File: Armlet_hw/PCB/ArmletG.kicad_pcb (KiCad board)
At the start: 2 copper layers, 93 x 35 mm, 86 parts, among them M1 MOTOR_NO_CONTACTS, Q1 LED_RGB 5050, Q2 BC848, Q3 MMBT2222, Q5 MMBT2222, SW1 DIPx6, SW2 BUTTON, SW4 SWITCH

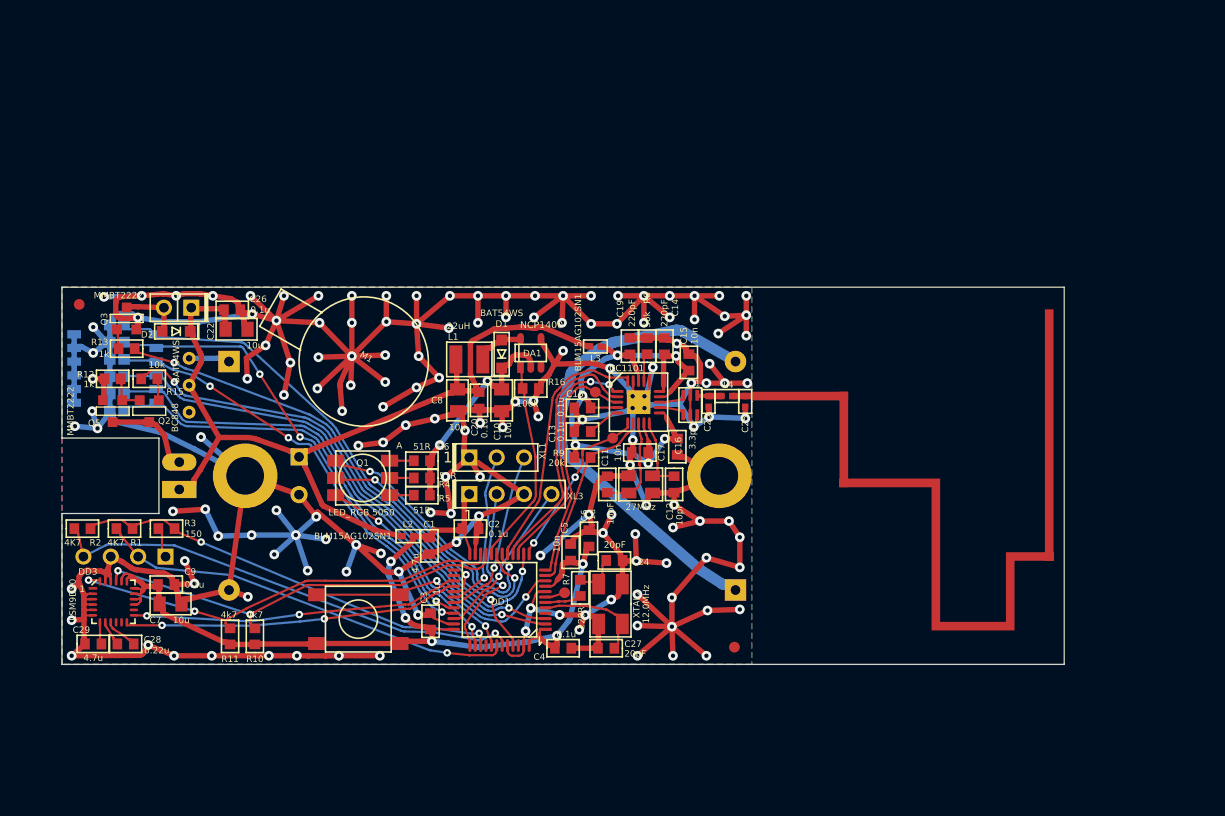
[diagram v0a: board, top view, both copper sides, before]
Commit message: 3 parts of armlet case
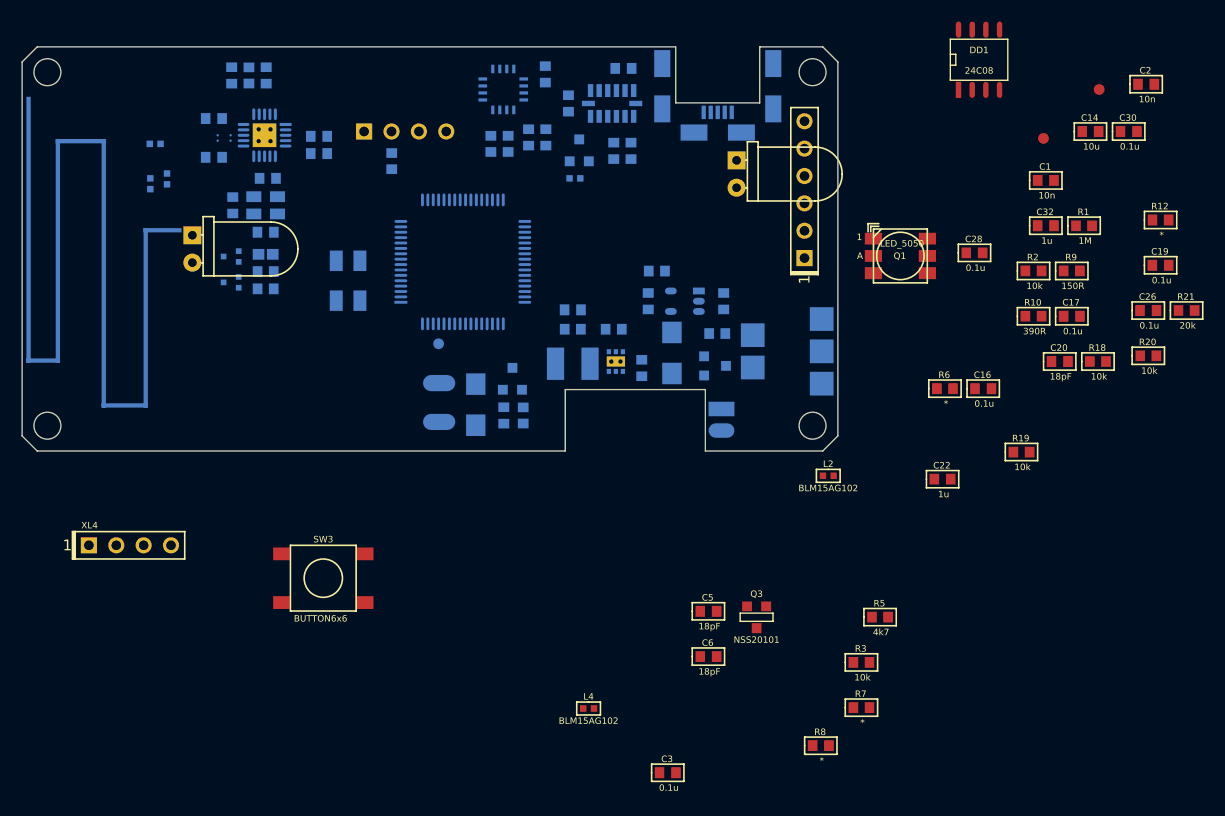
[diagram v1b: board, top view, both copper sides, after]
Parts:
- removed B1, B2: BAT, Installations:BATTERY_AAA_X1
- removed C23: 1.5pF, Capacitors:CAP_0402
- removed F2, F3, F4, F5, F6: Fuse0R, Resistors:RES_0603_FUSE
- removed HOLE1, HOLE2: HOLE_METALLED, PCB:Hole3_5_out6mm
- removed R15: 10k, Resistors:RES_0603
- removed RP1, RP2: REFPOINT, PCB:REF_POINT_1MM
- removed SW1: DIPx6, Switches:DIP_SMD_1D27X6
- removed SW2: BUTTON, Switches:BTN_6x6
- removed SW4: SWITCH, Switches:SW_SS-1P2T
- added C30: 0.1u, Capacitors:CAP_0603, F.Cu at (190.0, 76.1)
- added C31: 0.1u, Capacitors:CAP_0603, B.Cu at (143.8, 77.8)
- added C32: 1u, Capacitors:CAP_0603, F.Cu at (182.3, 84.8)
- added C33: 220pF, Capacitors:CAP_0603, B.Cu at (106.8, 70.8)
- added C34: *, Capacitors:CAP_0402, B.Cu at (99.7, 77.2)
- added C35: 10n, Capacitors:CAP_0603, B.Cu at (105.1, 74.8)
- added C36: 3.3pF, Capacitors:CAP_0603, B.Cu at (105.1, 78.5)
- added C37: *, Capacitors:CAP_0402, B.Cu at (100.8, 80.5)
- added C38: 10n, Capacitors:CAP_0603, B.Cu at (110.1, 80.4)
- added C39: 0.1u, Capacitors:CAP_0603, B.Cu at (114.8, 76.5)
- added C40: 220pF, Capacitors:CAP_0603, B.Cu at (110.0, 70.8)
- added D4: LED, LEDs:LED_Through-Hole-5mm-HOR, F.Cu at (103.1, 87.0)
- added DA2: NCP1529DFN, QFN_DFN:DFN6, B.Cu at (142.4, 97.4)
- added DD4: LSM303DLHC, LGA:14_5X3_P08, B.Cu at (142.1, 73.5)
- added DD5: CC1101, QFN_DFN:QFN20, B.Cu at (109.8, 76.4)
- added L5: *, Inductors:IND_0402, B.Cu at (99.2, 80.9)
- added Q4: IRLML9303, SOT:SOT23-3, B.Cu at (151.6, 97.8)
- added Q7: NSS20101, SOT:SC89-3, B.Cu at (106.7, 90.1)
- added Q8: NSS20101, SOT:SC89-3, B.Cu at (106.7, 87.7)
- added R14: 4k7, Resistors:RES_0603, B.Cu at (130.8, 77.2)
- added R17: 10k, Resistors:RES_0603, B.Cu at (151.8, 94.8)
- added R18: 10k, Resistors:RES_0603, F.Cu at (187.1, 97.4)
- added R19: 10k, Resistors:RES_0603, F.Cu at (180.0, 105.8)
- added R20: 10k, Resistors:RES_0603, F.Cu at (191.8, 96.9)
- added R21: 20k, Resistors:RES_0603, F.Cu at (195.4, 92.7)
- added R22: 390k, Resistors:RES_0603, B.Cu at (138.4, 94.4)
- added R23: 100k, Resistors:RES_0603, B.Cu at (142.2, 94.4)
- added R25: 56k, Resistors:RES_0603, B.Cu at (108.3, 70.8)
- added R26: 10k, Resistors:RES_0603, B.Cu at (109.9, 89.1)
- added R27: 1k, Resistors:RES_0603, B.Cu at (109.9, 90.7)
- added SW3: BUTTON6x6, BtnsSwitches:BTN_6x6, F.Cu at (115.2, 117.5)
- added XL2: CONN_4, Connectors:PBS-4R, B.Cu at (122.8, 76.1)
- added XL5: NOKIA_BAT, Connectors:CONN_NOKIA_ACC, B.Cu at (156.3, 96.5)
- added XL7: CONN_1, PCB:Oval3x1.5, B.Cu at (126.0, 99.4)
- ANT1: footprint Radio:ANT_868_MEANDER_4HOR_35mm -> Radio:ANT_868_ARMLETG; moved to B.Cu
- BLN1: value 0896BM15A0001 -> BALUN868ST; footprint Radio:BALUN_JOHANSON868 -> Radio:BALUN868_ST; moved to B.Cu
- C1: value 4.7u -> 10n
- C10: value 10u -> 10n; footprint Capacitors:CAP_0805 -> Capacitors:CAP_0603; moved to B.Cu
- C11: value 10pF -> 4.7u; moved to B.Cu
- C12: value 10pF -> 10u; moved to B.Cu
- C13, TP1: moved to B.Cu
- C14: value 220pF -> 10u
- C15: value 10n -> 18pF; moved to B.Cu
- C16: value 3.3pF -> 0.1u
- C17: value 10n -> 0.1u
- C18: value 0.1u -> 18pF; moved to B.Cu
- C19: value 220pF -> 0.1u
- C2: value 0.1u -> 10n
- C20: value 0.1u -> 18pF
- C21: value 1000u 6v3 -> 0.1u; footprint Capacitors:CAP_08xxR_HOR -> Capacitors:CAP_0603
- C22: value 10u -> 1u; footprint Capacitors:CAP_0805 -> Capacitors:CAP_0603
- C24: value 20pF -> 10u; moved to B.Cu
- C25: value DoNotMount -> 0.22u; footprint Capacitors:CAP_0402 -> Capacitors:CAP_0603; moved to B.Cu
- C27: value 20pF -> 4.7u; moved to B.Cu
- C28: value 0.22u -> 0.1u
- C29: value 4.7u -> 10u; moved to B.Cu
- C4: value 0.1u -> 4.7u; moved to B.Cu
- C5: value 10n -> 18pF
- C6: value 1u -> 18pF
- C7: value 10u -> 4.7u; footprint Capacitors:CAP_0805 -> Capacitors:CAP_0603; moved to B.Cu
- C8: value 10u -> 220u16V; footprint Capacitors:CAP_0805 -> Capacitors:CAP_05xxR_horiz_HOLE; moved to B.Cu
- C9: value 0.1u -> 10u; moved to B.Cu
- D1: value BAT54WS -> WhiteLED; footprint Diodes:SOD323 -> LEDs:LED_Through-Hole-5mm-HOR
- D2: value BAT54WS -> SS14; footprint Diodes:SOD323 -> Diodes:SMA_DO214AC; moved to B.Cu
- D3: value LED -> SS14; footprint LEDs:LED_SMD-5mm-HOR_mirr -> Diodes:SMA_DO214AC
- DA1: value NCP1400 -> MCP73832; moved to B.Cu
- DD1: value STM32L151CxTx -> 24C08; footprint LQFP:LQFP48 -> SO_DIL_TSSOP:SO8_150MIL
- DD2: value CC1101 -> STM32L476Rx; footprint QFN:QFN20 -> LQFP_TQFP:LQFP64; moved to B.Cu
- DD3: value LSM9DS0 -> L3GD20; footprint LGA:24_4X4_P05 -> LGA:16_4X4_P065; moved to B.Cu
- L1: value 22uH -> BLM15AG102; footprint Inductors:IND_1210_LQH32C -> Inductors:IND_0402; moved to B.Cu
- L2: value BLM15AG102SN1 -> BLM15AG102
- L3: value BLM15AG102SN1 -> 2.2uH; footprint Inductors:IND_0402 -> Inductors:IND_1515; moved to B.Cu
- L4: value 5.6nH -> BLM15AG102
- M1: footprint PCB:Motor_no_Contacts -> Installation:Motor_no_Contacts; moved to B.Cu
- Q1: value LED_RGB 5050 -> LED_5050; footprint LEDs:5050 -> LEDs:LED_5050
- Q2: value BC848 -> IRLML9303; moved to B.Cu
- Q3: value MMBT2222 -> NSS20101
- Q5: value MMBT2222 -> NSS20101; moved to B.Cu
- R1: value 4K7 -> 1M
- R10: value 4k7 -> 390R
- R11: value 4k7 -> 2k; moved to B.Cu
- R12: value 1k -> *
- R13: value 1k -> 4k7; moved to B.Cu
- R16: value 100k -> 1k; moved to B.Cu
- R2: value 4K7 -> 10k
- R3: value 150 -> 10k
- R4: value 51R -> 4k7; moved to B.Cu
- R5: value 51R -> 4k7
- R6: value 51R -> *
- R7: value 220R -> *
- R8: value 56k -> *
- R9: value 20k -> 150R
- XL1: value CONN_3 -> CONN_6; footprint Connectors:PLS-3 -> Connectors:PLS-6; moved to B.Cu
- XL3: value ST_SWD -> USB_Micro_B; footprint Connectors:PLS-4 -> Connectors:USBmicro_MOLEX_WM17142; moved to B.Cu
- XL4: footprint Connectors:PBS-4R -> Connectors:PLS-4; moved to F.Cu
- XL6: value CONN_2 -> CONN_1; footprint Connectors:PLS-2 -> PCB:Oval3x1.5; moved to B.Cu
- XTAL1: value 27MHz -> 12MHz; footprint Quartz:03225C4 -> Quartz:0503x4-4; moved to B.Cu
- XTAL2: value 12.0MHz -> 27MHz; footprint Quartz:0503x4-4 -> Quartz:03225C4; moved to B.Cu
- moved R12 98.4 mm to (192.9, 84.3)
- moved R1 93.4 mm to (185.8, 84.8)
- moved R2 91.4 mm to (181.2, 89.0)
- moved C28 86.7 mm to (175.7, 87.3), turned to 0 degrees
- moved C26 85.0 mm to (191.8, 92.7)
- moved R10 78.1 mm to (181.2, 93.2), turned to 0 degrees
- moved C2 75.0 mm to (191.6, 71.7)
- moved DD1 67.0 mm to (176.1, 69.4), turned to 0 degrees
- moved C22 67.0 mm to (172.7, 108.3)
- moved C29 66.5 mm to (142.2, 77.8), turned to 90 degrees
- moved C1 66.5 mm to (182.3, 80.6), turned to 0 degrees
- moved R3 65.7 mm to (165.2, 125.3)
- moved Q3 64.7 mm to (155.5, 121.1), turned to 0 degrees
- moved DD3 59.7 mm to (131.9, 72.2), turned to 90 degrees
- moved C7 58.5 mm to (152.4, 91.8), turned to 270 degrees
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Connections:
- C1 pad 1: PwrMCU -> GND
- C1 pad 2: GND -> /SHLD
- C10 pad 1: +3.3V -> GND
- C10 pad 2: GND -> Net-(C10-Pad2)
- C11 pad 1: Net-(C11-Pad1) -> GND
- C11 pad 2: GND -> PwrUnst
- C12 pad 1: Net-(C12-Pad1) -> GND
- C12 pad 2: GND -> /PWR_ACC
- C13 pad 1: Net-(C13-Pad1) -> GND
- C13 pad 2: GND -> /PWR_ACC
- C14 pad 1: VCC -> GND
- C14 pad 2: GND -> PwrMCU
- C15 pad 1: VCC -> Net-(C15-Pad1)
- C16 pad 1: VCC -> GND
- C16 pad 2: GND -> PwrMCU
- C17 pad 1: VCC -> GND
- C17 pad 2: GND -> PwrMCU
- C18 pad 1: VCC -> Net-(C18-Pad1)
- C19 pad 1: VCC -> GND
- C19 pad 2: GND -> PwrMCU
- C2 pad 1: PwrMCU -> GND
- C2 pad 2: GND -> +5V
- C20 pad 1: +BATT -> Net-(C20-Pad1)
- C20 pad 2: GND -> +3.3V
- C21 pad 1: +BATT -> GND
- C21 pad 2: GND -> Net-(C21-Pad2)
- C22 pad 1: +BATT -> GND
- C22 pad 2: GND -> PwrMCU
- C24 pad 1: Net-(C24-Pad1) -> GND
- C24 pad 2: GND -> +3.3V
- C25 pad 1: /ANT2 -> Net-(C25-Pad1)
- C25 pad 2: GND -> Net-(C25-Pad2)
- C26 pad 1: +BATT -> GND
- C26 pad 2: GND -> PwrMCU
- C27 pad 1: Net-(C27-Pad1) -> GND
- C27 pad 2: GND -> Net-(C27-Pad2)
- C28 pad 1: Net-(C28-Pad1) -> GND
- C28 pad 2: Net-(C28-Pad2) -> PwrMCU
- C29 pad 2: Net-(C29-Pad2) -> /PWR_ACC
- C3 pad 1: PwrMCU -> GND
- C3 pad 2: GND -> /PWR_EE
- C4 pad 1: PwrMCU -> GND
- C4 pad 2: GND -> +5V
- C5 pad 1: PwrMCU -> Net-(C5-Pad1)
- C6 pad 1: PwrMCU -> Net-(C6-Pad1)
- C7 pad 1: PwrMCU -> GND
- C7 pad 2: GND -> +BATT
- C9 pad 1: PwrMCU -> GND
- C9 pad 2: GND -> +3.3V
- D1 pad A: /Lout -> PwrUnst
- D1 pad C: +3.3V -> Net-(D1-PadC)
- D2 pad A: /VibroOut -> +5V
- D2 pad C: +BATT -> PwrUnst
- D3 pad A: +BATT -> /VIBRO_OUT
- D3 pad C: /IR_LED_OUT -> +3.3V
- DA1 pad 1: /LED_EN -> /Charge
- DA1 pad 2: +3.3V -> GND
- DA1 pad 3: (no net) -> +BATT
- DA1 pad 4: GND -> +5V
- DA1 pad 5: /Lout -> Net-(DA1-Pad5)
- DD1 pad 1: PwrMCU -> GND
- DD1 pad 2: /DS2 -> GND
- DD1 pad 3: /DS3 -> GND
- DD1 pad 4: (no net) -> GND
- DD1 pad 5: Net-(C27-Pad1) -> /SDA_EE
- DD1 pad 6: Net-(DD1-Pad6) -> /SCL_EE
- DD1 pad 7: Net-(DD1-Pad7) -> GND
- DD1 pad 8: GND -> /PWR_EE
- DD2 pad 1: /CC_SCK -> PwrMCU
- DD2 pad 10: Net-(C12-Pad1) -> /PWR_EE
- DD2 pad 11: VCC -> (no net)
- DD2 pad 12: /RF1 -> GND
- DD2 pad 13: /RF2 -> PwrMCU
- DD2 pad 14: VCC -> /CC_GDO0
- DD2 pad 15: VCC -> /CC_CS
- DD2 pad 16: GND -> /UART_TX
- DD2 pad 17: Net-(DD2-Pad17) -> /UART_RX
- DD2 pad 18: VCC -> GND
- DD2 pad 19: GND -> PwrMCU
- DD2 pad 2: /CC_MISO -> Net-(DD2-Pad2)
- DD2 pad 20: /CC_MOSI -> /IR_OUT_DAC
- DD2 pad 3: /CC_GDO2 -> (no net)
- DD2 pad 4: VCC -> (no net)
- DD2 pad 5: Net-(C13-Pad1) -> Net-(C5-Pad1)
- DD2 pad 6: /CC_GDO0 -> Net-(DD2-Pad6)
- DD2 pad 7: /CC_CS -> Net-(DD2-Pad7)
- DD2 pad 8: Net-(C11-Pad1) -> /SCL_EE
- DD2 pad 9: VCC -> /SDA_EE
- DD3 pad 1: (no net) -> /PWR_ACC
- DD3 pad 10: (no net) -> GND
- DD3 pad 11: (no net) -> GND
- DD3 pad 12: /GYRO_DRDY -> GND
- DD3 pad 13: /ACC_INT1 -> GND
- DD3 pad 14: (no net) -> Net-(C10-Pad2)
- DD3 pad 15: PwrMCU -> /PWR_ACC
- DD3 pad 16: PwrMCU -> /PWR_ACC
- DD3 pad 2: GND -> /SCL_ACC
- DD3 pad 3: GND -> /SDA_ACC
- DD3 pad 4: GND -> /PWR_ACC
- DD3 pad 5: GND -> /PWR_ACC
- DD3 pad 6: GND -> /GYRO_DRDY
- DD3 pad 7: Net-(C29-Pad2) -> (no net)
- DD3 pad 8: Net-(C28-Pad2) -> GND
- DD3 pad 9: Net-(C28-Pad1) -> GND
- F1 pad 1: /DS1 -> Net-(F1-Pad1)
- F1 pad 2: GND -> /IR_OUT_TIM
- L1 pad 1: /Lout -> Net-(L1-Pad1)
- L1 pad 2: +BATT -> +3.3V
- L2 pad 2: +BATT -> +3.3V
- L3 pad 1: VCC -> +3.3V
- L3 pad 2: +BATT -> /Lout3V3
- L4 pad 1: /ANT2 -> VCC
- L4 pad 2: /ANT1 -> +3.3V
- Q2 pad 1: Net-(Q2-Pad1) -> /PWR_ACC_CTRL
- Q2 pad 2: Net-(Q2-Pad2) -> Net-(L1-Pad1)
- Q2 pad 3: /IR_LED_OUT -> /PWR_ACC
- Q3 pad 3: /VibroOut -> Net-(D1-PadC)
- Q5 pad 1: Net-(Q2-Pad2) -> Net-(Q5-Pad1)
- Q5 pad 3: /IR_LED_OUT -> /VIBRO_OUT
- R1 pad 1: /P_SCL -> /SHLD
- R1 pad 2: /PeriphPwr -> GND
- R10 pad 1: PwrMCU -> Net-(C6-Pad1)
- R10 pad 2: /I2C_SCL -> Net-(DD2-Pad6)
- R11 pad 1: /I2C_SDA -> Net-(DA1-Pad5)
- R11 pad 2: PwrMCU -> GND
- R12 pad 1: GND -> Net-(Q3-Pad1)
- R12 pad 2: Net-(Q2-Pad2) -> /LEDW_CTRL
- R13 pad 1: /Vibro -> /PWR_ACC
- R13 pad 2: Net-(Q3-Pad1) -> /SCL_ACC
- R16 pad 1: /LED_EN -> /Vibro
- R16 pad 2: GND -> Net-(Q5-Pad1)
- R2 pad 1: /P_SDA -> /PWR_EE
- R2 pad 2: /PeriphPwr -> /SDA_EE
- R3 pad 1: /PeriphPwr1 -> /SCL_EE
- R3 pad 2: /PeriphPwr -> /PWR_EE
- R4 pad 1: +3.3V -> /PWR_PILL
- R4 pad 2: Net-(Q1-PadRA) -> /SCL_PILL
- R5 pad 1: +3.3V -> /PWR_PILL
- R5 pad 2: Net-(Q1-PadGA) -> /SDA_PILL
- R6 pad 1: +3.3V -> Net-(Q1-Pad6)
- R6 pad 2: Net-(Q1-PadBA) -> /BLUE_LED
- R7 pad 1: Net-(DD1-Pad6) -> Net-(Q1-Pad5)
- R7 pad 2: Net-(C24-Pad1) -> /RED_LED
- R8 pad 1: Net-(DD2-Pad17) -> Net-(Q1-Pad4)
- R8 pad 2: GND -> /GREEN_LED
- R9 pad 1: /CC_CS -> /PWR_PILL
- R9 pad 2: VCC -> /PWR_PILL_PROT
- TP1 pad 1: Net-(DD1-Pad7) -> Net-(DD2-Pad61)
- TP2 pad 1: /CC_GDO0 -> Net-(DD2-Pad7)
- TP3 pad 1: /CC_GDO2 -> /CC_GDO0
- XL1 pad 1: GND -> PwrMCU
- XL1 pad 2: /UART_TX -> /SWCLK
- XL1 pad 3: /UART_RX -> GND
- XL3 pad 1: PwrMCU -> +5V
- XL3 pad 2: /SWCLK -> /D-
- XL3 pad 3: GND -> /D+
- XL3 pad 4: /SWDIO -> GND
- XL4 pad 1: /PeriphPwr1 -> GND
- XL4 pad 2: /P_SCL -> Net-(DD2-Pad26)
- XL4 pad 3: GND -> Net-(DD2-Pad27)
- XL4 pad 4: /P_SDA -> Net-(DD2-Pad28)
- XL6 pad 1: +BATT -> +3.3V
- XTAL1 pad 1: Net-(C11-Pad1) -> Net-(C5-Pad1)
- XTAL1 pad 2: Net-(C12-Pad1) -> Net-(C6-Pad1)
- XTAL2 pad 1: Net-(C24-Pad1) -> Net-(C15-Pad1)
- XTAL2 pad 2: Net-(C27-Pad1) -> Net-(C18-Pad1)
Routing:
- net GND: track 646.6 -> 0.00 mm, vias 154 -> 0
- net PwrMCU: track 98.4 -> 0.00 mm, vias 5 -> 0
- net +BATT: track 83.1 -> 0.00 mm
- net VCC: track 58.5 -> 0.00 mm, vias 6 -> 0
- net /DS2: track 48.5 -> 0.00 mm, vias 1 -> 0
- net /IR_LED: track 48.3 -> 0.00 mm, vias 2 -> 0
- net /DS3: track 48.2 -> 0.00 mm, vias 1 -> 0
- net /Vibro: track 46.7 -> 0.00 mm, vias 2 -> 0
- net /BAT_BTW: track 45.2 -> 0.00 mm
- net /P_SDA: track 44.3 -> 0.00 mm, vias 1 -> 0
- net /DS1: track 43.9 -> 0.00 mm, vias 1 -> 0
- net /DS6: track 43.9 -> 0.00 mm, vias 1 -> 0
- net /DS5: track 43.1 -> 0.00 mm, vias 3 -> 0
- net /I2C_SDA: track 41.0 -> 0.00 mm, vias 2 -> 0
- net /DS4: track 40.6 -> 0.00 mm, vias 3 -> 0
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- removed copper zone on B.Cu, net GND
- removed copper zone on F.Cu, net GND
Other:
- board size 93 x 35 mm -> 75.7 x 37.5 mm
- net class Ant removed
- net class Default: trace_width 0.2 -> 0.25; via_dia 0.7 -> 0.6; via_drill 0.3 -> 0.4
- net class Wide removed
- rule pad_to_mask_clearance: 0.1 -> 0
- board text removed: "1 0"

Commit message: Layout completed
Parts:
- C1, C14, C16, C17, C19, C2, C20, C22, C26, C28, C3, C30, C32, C5, C6, DD1, L2, L4, Q3, R1, R10, R12, R18, R19, R2, R20, R21, R3, R5, R6, R7, R8, R9, TP2, TP3: moved to B.Cu
- moved R21 82.7 mm to (113.2, 83.2), turned to 270 degrees
- moved C26 71.3 mm to (120.6, 88.8)
- moved TP3 69.4 mm to (112.8, 80.6)
- moved C30 68.6 mm to (121.4, 79.0), turned to 270 degrees
- moved TP2 66.9 mm to (121.4, 84.2)
- moved XL4 62.2 mm to (136.6, 69.6)
- moved C32 61.0 mm to (121.4, 82.0), turned to 90 degrees
- moved L4 60.5 mm to (113.4, 75.2)
- moved R10 60.1 mm to (121.4, 86.4), turned to 90 degrees
- moved C19 56.8 mm to (136.2, 91.2), turned to 90 degrees
- moved C3 56.7 mm to (140.8, 79.2)
- moved C16 55.4 mm to (126.2, 76.6)
- moved C6 54.3 mm to (115.4, 83.8), turned to 90 degrees
- moved C5 53.2 mm to (118.0, 78.8), turned to 180 degrees
- moved C28 52.6 mm to (123.2, 91.4)
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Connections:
- XL5 pad H: (no net) -> GND

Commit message: Tracing done
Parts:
- moved C5 11.4 mm to (117.4, 90.2), turned to 0 degrees
- moved L4 10.0 mm to (113.6, 85.2), turned to 270 degrees
- moved XTAL1 3.26 mm to (117.8, 86.0), turned to 90 degrees
- moved C24 3.05 mm to (139.2, 91.2)
- moved C6 2.97 mm to (117.6, 81.8), turned to 180 degrees
- moved C19 2.41 mm to (134.1, 92.3), turned to 0 degrees
- moved L2 2.28 mm to (136.6, 92.6)
- moved R26 2.15 mm to (110.8, 87.8)
- moved R10 1.74 mm to (120.6, 84.8), turned to 270 degrees
- moved F1 1.71 mm to (110.8, 89.6)
- moved R14 1.70 mm to (135.0, 75.4)
- moved TP3 1.66 mm to (111.3, 80.0)
- moved R7 1.60 mm to (142.6, 85.8)
- moved R8 1.60 mm to (142.6, 87.4)
- moved R13 1.50 mm to (133.4, 75.4)
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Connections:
- net /Vibro renamed /Vibro_CTRL
- net Net-(D1-PadC) renamed /LEDW_OUT
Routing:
- net GND: track 0.00 -> 569.2 mm, vias 0 -> 137
- net +3.3V: track 0.00 -> 111.9 mm, vias 0 -> 3
- net PwrMCU: track 0.00 -> 103.4 mm, vias 0 -> 10
- net PwrUnst: track 0.00 -> 86.9 mm, vias 0 -> 4
- net VCC: track 0.00 -> 61.3 mm, vias 0 -> 8
- net /PWR_ACC: track 0.00 -> 45.1 mm, vias 0 -> 2
- net +5V: track 0.00 -> 39.5 mm, vias 0 -> 2
- net /UART_TX: track 0.00 -> 38.6 mm, vias 0 -> 1
- net /UART_RX: track 0.00 -> 38.1 mm, vias 0 -> 1
- net +BATT: track 0.00 -> 37.1 mm, vias 0 -> 2
- net /SDA_ACC: track 0.00 -> 36.9 mm, vias 0 -> 3
- net /SCL_ACC: track 0.00 -> 34.6 mm, vias 0 -> 3
- net /SHLD: track 0.00 -> 32.4 mm, vias 0 -> 3
- net /SWCLK: track 0.00 -> 28.1 mm, vias 0 -> 1
- net Net-(DD2-Pad24): track 0.00 -> 27.1 mm, vias 0 -> 2
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- added copper zone on B.Cu, net GND
- added copper zone on F.Cu, net GND
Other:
- net class Default: trace_width 0.25 -> 0.2; via_dia 0.6 -> 0.7; via_drill 0.4 -> 0.3
- net class Wide added: clearance 0.2, trace_width 0.5, via_dia 0.9, via_drill 0.4

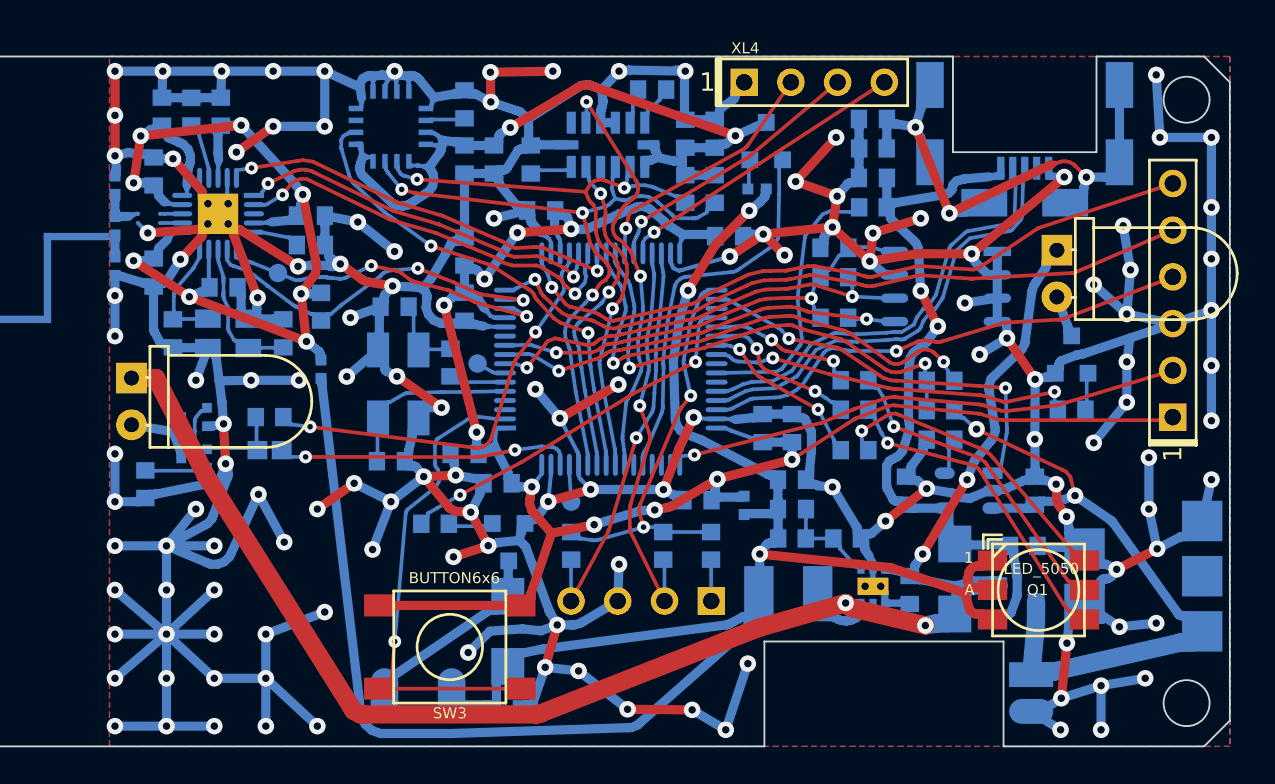
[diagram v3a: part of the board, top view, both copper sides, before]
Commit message: + Armlet PCB sent to factory. * NSS 20101 footprints corrected to SC89-3 * Switched back to TopoR 6.1
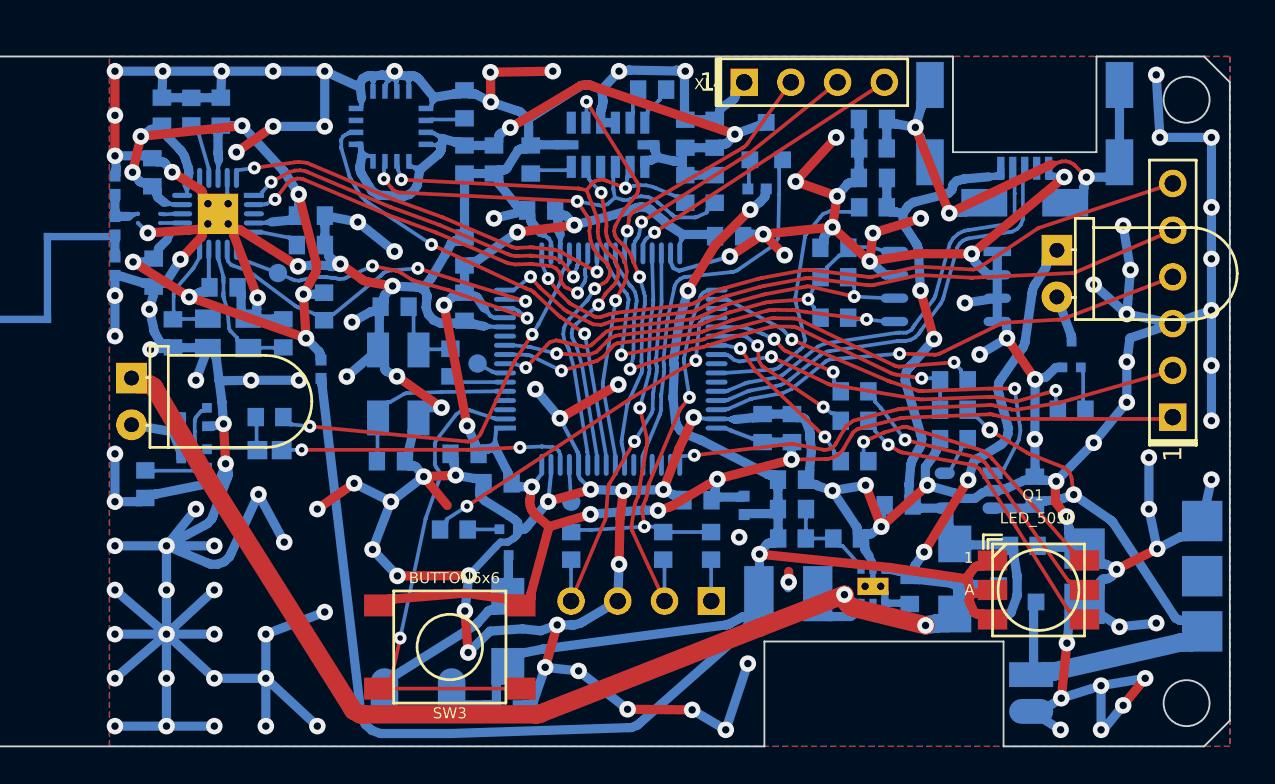
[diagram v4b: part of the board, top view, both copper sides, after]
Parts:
- Q3, Q5: footprint SOT:SOT23-3 -> SOT:SC89-3
- moved R16 1.07 mm to (120.8, 93.9)
- moved C4 0.89 mm to (145.0, 92.6), turned to 0 degrees
- moved R19 0.73 mm to (148.0, 85.8)
- moved R20 0.73 mm to (148.0, 87.4)
- moved R11 0.72 mm to (148.0, 89.0)
- moved R6 0.60 mm to (142.6, 90.2)
- moved R7 0.60 mm to (142.6, 86.4)
- moved R8 0.60 mm to (142.6, 88.0)
- moved R21 0.17 mm to (113.8, 81.8)
- moved C35 0.08 mm to (104.4, 74.5)
- turned Q3 to 90 degrees
- turned Q5 to 270 degrees
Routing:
- net GND: track 569.2 -> 598.1 mm, vias 137 -> 144
- net +3.3V: track 111.9 -> 116.7 mm
- net PwrUnst: track 86.9 -> 88.9 mm
- net +5V: track 39.5 -> 37.8 mm
- net /SDA_ACC: track 36.9 -> 38.0 mm
- net Net-(DD2-Pad24): track 27.1 -> 26.1 mm
- net PwrMCU: track 103.4 -> 102.5 mm, vias 10 -> 9
- net /IR_OUT_DAC: track 23.0 -> 22.1 mm
- net /Charge: track 21.9 -> 22.7 mm
- net /Vibro_CTRL: track 20.6 -> 19.8 mm
- net VCC: track 61.3 -> 60.6 mm
- net /PWR_ACC: track 45.1 -> 44.5 mm
- net Net-(Q5-Pad1): track 2.41 -> 1.73 mm
- net Net-(Q1-Pad6): track 16.7 -> 16.2 mm
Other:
- rule pad_to_mask_clearance: 0 -> 0.1
- board text added: "ArmletG 01"

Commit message: PCB2 done
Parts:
- removed C27: 4.7u, Capacitors:CAP_0603
- added C23: 10u, Capacitors:CAP_0603, B.Cu at (125.4, 74.2)
- added Logo1: Logo, Pictures:Ostranna_16d9_13d5, B.Cu at (94.5, 93.4)
- added SW1: IT-1187U, BtnsSwitches:BTN_4x4_SMD, F.Cu at (120.6, 100.4)
- added XL8: CONN_4, Connectors:PLS-4, B.Cu at (157.3, 87.8)
- BLN1: value BALUN868ST -> BALUN868JOHANSON; footprint Radio:BALUN868_ST -> Radio:BALUN_JOHANSON868
- C11, C4, C7: value 4.7u -> 10u
- D2, D3: value SS14 -> PMEG2020; footprint Diodes:SMA_DO214AC -> Diodes:SOD323
- R11: value 2k -> 3k
- XL4: value CONN_4 -> CONN_5; footprint Connectors:PLS-4 -> Connectors:PLS-5; moved to B.Cu
- moved XL4 2.31 mm to (134.3, 69.6)
- moved L4 1.79 mm to (114.4, 86.8)
- moved R21 0.82 mm to (114.6, 81.6)
- moved BLN1 0.81 mm to (104.1, 76.8)
- moved C25 0.60 mm to (131.0, 70.0)
- moved C35 0.58 mm to (104.7, 74.0)
- moved Q1 0.50 mm to (152.6, 96.7), turned to 180 degrees
- moved C15 0.45 mm to (112.0, 83.0)
- moved C18 0.45 mm to (106.0, 83.0)
- moved C21 0.45 mm to (113.5, 78.2)
- moved C36 0.45 mm to (104.9, 79.8)
- moved C38 0.45 mm to (108.7, 80.5)
- moved R25 0.45 mm to (107.0, 71.0)
- moved TP3 0.45 mm to (111.7, 79.8)
- moved XTAL2 0.45 mm to (109.0, 83.0)
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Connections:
- DD2 pad 28: Net-(DD2-Pad28) -> (no net)
- DD2 pad 35: (no net) -> /Vibro_CTRL
- DD2 pad 36: /Vibro_CTRL -> Net-(DD2-Pad36)
- XL4 pad 4: Net-(DD2-Pad28) -> Net-(DD2-Pad36)
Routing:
- net GND: track 598.1 -> 560.9 mm, vias 144 -> 138
- net Net-(DD2-Pad36): track 0.00 -> 19.4 mm
- net Net-(DD2-Pad28): track 16.3 -> 0.00 mm, vias 1 -> 0
- net PwrUnst: track 88.9 -> 102.2 mm
- net Net-(Q1-Pad5): track 16.8 -> 29.2 mm, vias 1 -> 2
- net +3.3V: track 116.7 -> 127.2 mm
- net Net-(Q1-Pad4): track 17.0 -> 26.3 mm, vias 1 -> 2
- net Net-(Q1-Pad6): track 16.2 -> 24.1 mm
- net /UART_TX: track 38.4 -> 40.8 mm
- net Net-(DD2-Pad2): track 26.5 -> 24.5 mm
- net PwrMCU: track 102.5 -> 100.5 mm
- net Net-(DD2-Pad27): track 14.9 -> 13.0 mm
- net Net-(DD2-Pad25): track 26.1 -> 27.8 mm
- net Net-(DD2-Pad24): track 26.1 -> 27.7 mm
- net /SHLD: track 32.4 -> 31.0 mm
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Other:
- board text added: "ArmletG 02"
- board text added: "Ostranna"
- board text removed: "ArmletG 01"
